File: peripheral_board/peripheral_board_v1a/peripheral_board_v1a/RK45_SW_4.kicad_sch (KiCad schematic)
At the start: 7 parts, among them J9 RJ45_Pulse_JXD6-0001NL

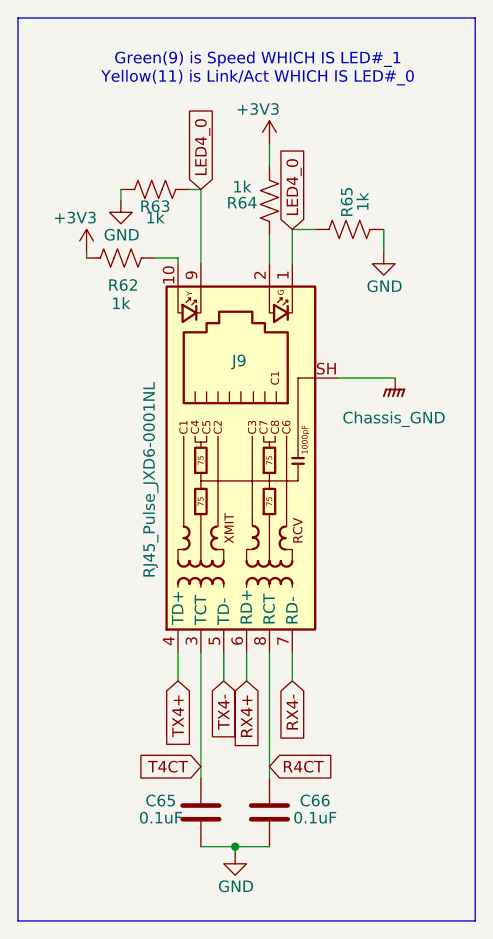
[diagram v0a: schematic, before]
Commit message: PCB Update
Got all the parts on the board placed. Now just finishing the routing for each interconnection.
Trying to maintain a side to side/up to down but the board kinda follows it. For each plane  there is fill zones that will be for the chip that is on the top. Some of the traces are just being fed to where they need to go but the important EMI signals are being contained to their guidelines.
I will need to look at the lengths of the traces to make sure they are kept around the same length.

Will need to go over the board with some other eyes to make sure its ok.

I made sure the Wiznet traces are the same as SALAD.
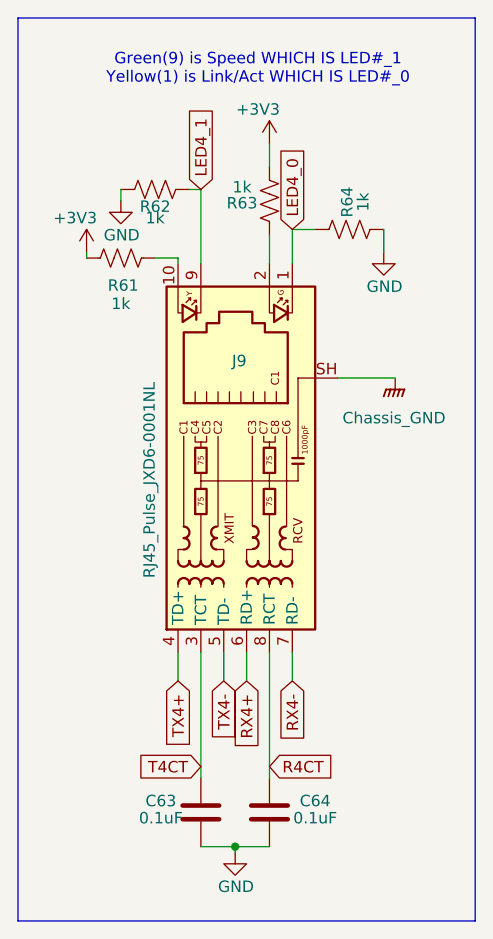
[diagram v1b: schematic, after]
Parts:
- renumbered C65 to C63, C66 to C64, R62 to R61, R63 to R62, R64 to R63, R65 to R64
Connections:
- net LED4_0: no longer J9.9, R62.1
- new net LED4_1: J9.9, R62.1
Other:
- note added: "Green(9) is Speed WHICH IS LED#_1 Yellow(1) is Link/Act WHICH IS LED#_0"
- note removed: "Green(9) is Speed WHICH IS LED#_1 Yellow(11) is Link/Act WHICH IS LED#_0"

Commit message: PCB almost done
Finished the routing except for the power board connector. Will be looking into adding in a Power path controller or similar. Want to add in via stitching for the DP signals. Should be just about done it would be more of just doing some change/improvements.
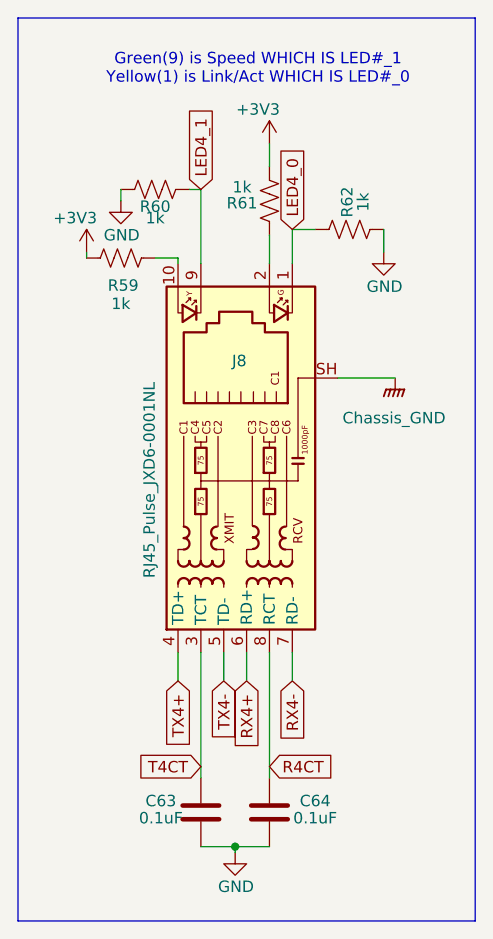
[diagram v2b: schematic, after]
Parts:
- renumbered J9 to J8, R61 to R59, R62 to R60, R63 to R61, R64 to R62
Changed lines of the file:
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@@
 		(on_board yes)
 		(dnp no)
-		(property "Reference" "#PWR0155"
+		(property "Reference" "#PWR0151"
 			(at 47.625 64.77 0)
 			(effects
@@
 			(project "peripheral_board"
 				(path "/14f8712f-1710-40cb-b01e-cc9b3c4405bd/bdffb641-9271-40a7-b849-e20d9ae38619/3055d292-9ba1-46a2-a820-6dedf7f46661"
-					(reference "#PWR0155")
+					(reference "#PWR0151")
 					(unit 1)
 				)
@@
 		(on_board yes)
 		(dnp no)
-		(property "Reference" "#PWR0157"
+		(property "Reference" "#PWR0153"
 			(at 64.135 55.88 0)
 			(effects
@@
 			(project "peripheral_board"
 				(path "/14f8712f-1710-40cb-b01e-cc9b3c4405bd/bdffb641-9271-40a7-b849-e20d9ae38619/3055d292-9ba1-46a2-a820-6dedf7f46661"
-					(reference "#PWR0157")
+					(reference "#PWR0153")
 					(unit 1)
 				)
@@
 		(on_board yes)
 		(dnp no)
-		(property "Reference" "R63"
+		(property "Reference" "R61"
 			(at 61.087 58.674 0)
 			(effects
@@
 			(project "peripheral_board"
 				(path "/14f8712f-1710-40cb-b01e-cc9b3c4405bd/bdffb641-9271-40a7-b849-e20d9ae38619/3055d292-9ba1-46a2-a820-6dedf7f46661"
-					(reference "R63")
+					(reference "R61")
 					(unit 1)
 				)
@@
 		(on_board yes)
 		(dnp no)
-		(property "Reference" "R64"
+		(property "Reference" "R62"
 			(at 72.771 58.547 0)
 			(effects
@@
 			(project "peripheral_board"
 				(path "/14f8712f-1710-40cb-b01e-cc9b3c4405bd/bdffb641-9271-40a7-b849-e20d9ae38619/3055d292-9ba1-46a2-a820-6dedf7f46661"
-					(reference "R64")
+					(reference "R62")
 					(unit 1)
 				)
@@
 		(on_board yes)
 		(dnp no)
-		(property "Reference" "#PWR0158"
+		(property "Reference" "#PWR0154"
 			(at 76.835 70.485 0)
 			(effects
@@
 			(project "peripheral_board"
 				(path "/14f8712f-1710-40cb-b01e-cc9b3c4405bd/bdffb641-9271-40a7-b849-e20d9ae38619/3055d292-9ba1-46a2-a820-6dedf7f46661"
-					(reference "#PWR0158")
+					(reference "#PWR0154")
 					(unit 1)
 				)
@@
 		(dnp no)
 		(fields_autoplaced yes)
-		(property "Reference" "#PWR0159"
+		(property "Reference" "#PWR0155"
 			(at 78.105 83.185 0)
 			(effects
@@
 			(project "peripheral_board"
 				(path "/14f8712f-1710-40cb-b01e-cc9b3c4405bd/bdffb641-9271-40a7-b849-e20d9ae38619/3055d292-9ba1-46a2-a820-6dedf7f46661"
-					(reference "#PWR0159")
+					(reference "#PWR0155")
 					(unit 1)
 				)
@@
 		(on_board yes)
 		(dnp no)
-		(property "Reference" "J9"
+		(property "Reference" "J8"
 			(at 61.595 76.2 90)
 			(effects
@@
 			(project "peripheral_board"
 				(path "/14f8712f-1710-40cb-b01e-cc9b3c4405bd/bdffb641-9271-40a7-b849-e20d9ae38619/3055d292-9ba1-46a2-a820-6dedf7f46661"
-					(reference "J9")
+					(reference "J8")
 					(unit 1)
 				)
@@
 		(on_board yes)
 		(dnp no)
-		(property "Reference" "R62"
+		(property "Reference" "R60"
 			(at 51.435 59.055 90)
 			(effects
@@
 			(project "peripheral_board"
 				(path "/14f8712f-1710-40cb-b01e-cc9b3c4405bd/bdffb641-9271-40a7-b849-e20d9ae38619/3055d292-9ba1-46a2-a820-6dedf7f46661"
-					(reference "R62")
+					(reference "R60")
 					(unit 1)
 				)
@@
 		(on_board yes)
 		(dnp no)
-		(property "Reference" "#PWR0156"
+		(property "Reference" "#PWR0152"
 			(at 60.325 137.16 0)
 			(effects
@@
 			(project "peripheral_board"
 				(path "/14f8712f-1710-40cb-b01e-cc9b3c4405bd/bdffb641-9271-40a7-b849-e20d9ae38619/3055d292-9ba1-46a2-a820-6dedf7f46661"
-					(reference "#PWR0156")
+					(reference "#PWR0152")
 					(unit 1)
 				)
@@
 		(on_board yes)
 		(dnp no)
-		(property "Reference" "#PWR0154"
+		(property "Reference" "#PWR0150"
 			(at 43.815 67.945 0)
 			(effects
@@
 			(project "peripheral_board"
 				(path "/14f8712f-1710-40cb-b01e-cc9b3c4405bd/bdffb641-9271-40a7-b849-e20d9ae38619/3055d292-9ba1-46a2-a820-6dedf7f46661"
-					(reference "#PWR0154")
+					(reference "#PWR0150")
 					(unit 1)
 				)
@@
 		(on_board yes)
 		(dnp no)
-		(property "Reference" "R61"
+		(property "Reference" "R59"
 			(at 47.879 67.818 90)
 			(effects
@@
 			(project "peripheral_board"
 				(path "/14f8712f-1710-40cb-b01e-cc9b3c4405bd/bdffb641-9271-40a7-b849-e20d9ae38619/3055d292-9ba1-46a2-a820-6dedf7f46661"
-					(reference "R61")
-					(unit 1)
-				)
+					(reference "R59")
+					(unit 1)
+				)

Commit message: Part picking for board
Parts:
- C63, C64: value 0.1uF -> 100nF
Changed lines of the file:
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@@
 			)
 		)
-		(property "Value" "0.1uF"
+		(property "Value" "100nF"
 			(at 69.215 127 0)
 			(effects
@@
 			)
 		)
-		(property "Value" "0.1uF"
+		(property "Value" "100nF"
 			(at 52.07 127 0)
 			(effects
